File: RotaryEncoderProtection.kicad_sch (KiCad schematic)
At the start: 14 parts, among them J1 DE9_Plug_MountingHoles, J2 Conn_01x01, J3 Conn_01x04

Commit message: removed traces, where zones are; added text, logos, copyright; added Reichelt article numbvers
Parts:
- C1: Reichelt.de (none) -> X7R-G0805 100N
- C2: Reichelt.de (none) -> RAD 22/35
- D1: Reichelt.de (none) -> 1N 4148W DIO
- D2, D3, D4: Reichelt.de (none) -> SMD ZF 24
- J1: Reichelt.de (none) -> D-SUB ST 09US
- R1: Reichelt.de (none) -> SMD-0805 22,0
- R2, R3, R4, R5: Reichelt.de (none) -> SMD-0805 10,0K
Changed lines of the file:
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@@
+			)
+		)
+		(property "Reichelt.de" "SMD-0805 10,0K"
+			(at 83.82 63.5 0)
+			(effects
+				(font
+					(size 1.27 1.27)
+				)
+				(hide yes)
 			)
 		)
@@
 			)
 		)
+		(property "Reichelt.de" "SMD-0805 10,0K"
+			(at 118.11 53.34 0)
+			(effects
+				(font
+					(size 1.27 1.27)
+				)
+				(hide yes)
+			)
+		)
 		(pin "2"
 		)
@@
 			)
 		)
+		(property "Reichelt.de" "SMD ZF 24"
+			(at 118.11 77.47 90)
+			(effects
+				(font
+					(size 1.27 1.27)
+				)
+				(hide yes)
+			)
+		)
 		(pin "2"
 		)
@@
 			)
 		)
-		(property "Datasheet" "~"
+		(property "Datasheet" "https://cdn-reichelt.de/documents/datenblatt/C120/DBR1-MXX-L.pdf"
 			(at 62.23 68.58 0)
 			(effects
@@
 			)
 		)
+		(property "Reichelt.de" "D-SUB ST 09US"
+			(at 62.23 68.58 0)
+			(effects
+				(font
+					(size 1.27 1.27)
+				)
+				(hide yes)
+			)
+		)
 		(pin "0"
 		)
@@
 			)
 		)
+		(property "Reichelt.de" "X7R-G0805 100N"
+			(at 132.08 53.34 0)
+			(effects
+				(font
+					(size 1.27 1.27)
+				)
+				(hide yes)
+			)
+		)
 		(pin "1"
 		)
@@
 		)
 		(property "Description" "Resistor"
+			(at 83.82 71.12 0)
+			(effects
+				(font
+					(size 1.27 1.27)
+				)
+				(hide yes)
+			)
+		)
+		(property "Reichelt.de" "SMD-0805 10,0K"
 			(at 83.82 71.12 0)
 			(effects
@@
 			)
 		)
+		(property "Reichelt.de" "SMD-0805 22,0"
+			(at 96.52 43.18 0)
+			(effects
+				(font
+					(size 1.27 1.27)
+				)
+				(hide yes)
+			)
+		)
 		(pin "2"
 		)
@@
 			)
 		)
+		(property "Reichelt.de" "SMD ZF 24"
+			(at 156.21 53.34 90)
+			(effects
+				(font
+					(size 1.27 1.27)
+				)
+				(hide yes)
+			)
+		)
 		(pin "2"
 		)
@@
 			)
 		)
+		(property "Reichelt.de" "1N 4148W DIO"
+			(at 81.28 43.18 0)
+			(effects
+				(font
+					(size 1.27 1.27)
+				)
+				(hide yes)
+			)
+		)
 		(pin "1"
 		)
@@
 			)
 		)
+		(property "Reichelt.de" "RAD 22/35"
+			(at 144.78 53.34 0)
+			(effects
+				(font
+					(size 1.27 1.27)
+				)
+				(hide yes)
+			)
+		)
 		(pin "2"
 		)
@@
 			)
 		)
+		(property "Reichelt.de" "SMD-0805 10,0K"
+			(at 104.14 53.34 0)
+			(effects
+				(font
+					(size 1.27 1.27)
+				)
+				(hide yes)
+			)
+		)
 		(pin "2"
 		)
@@
 			(effects
 				(font
+					(size 1.27 1.27)
+				)
+				(hide yes)
+			)
+		)
+		(property "Reichelt.de" "SMD ZF 24"
+			(at 104.14 77.47 90)
+			(effects
+				(font

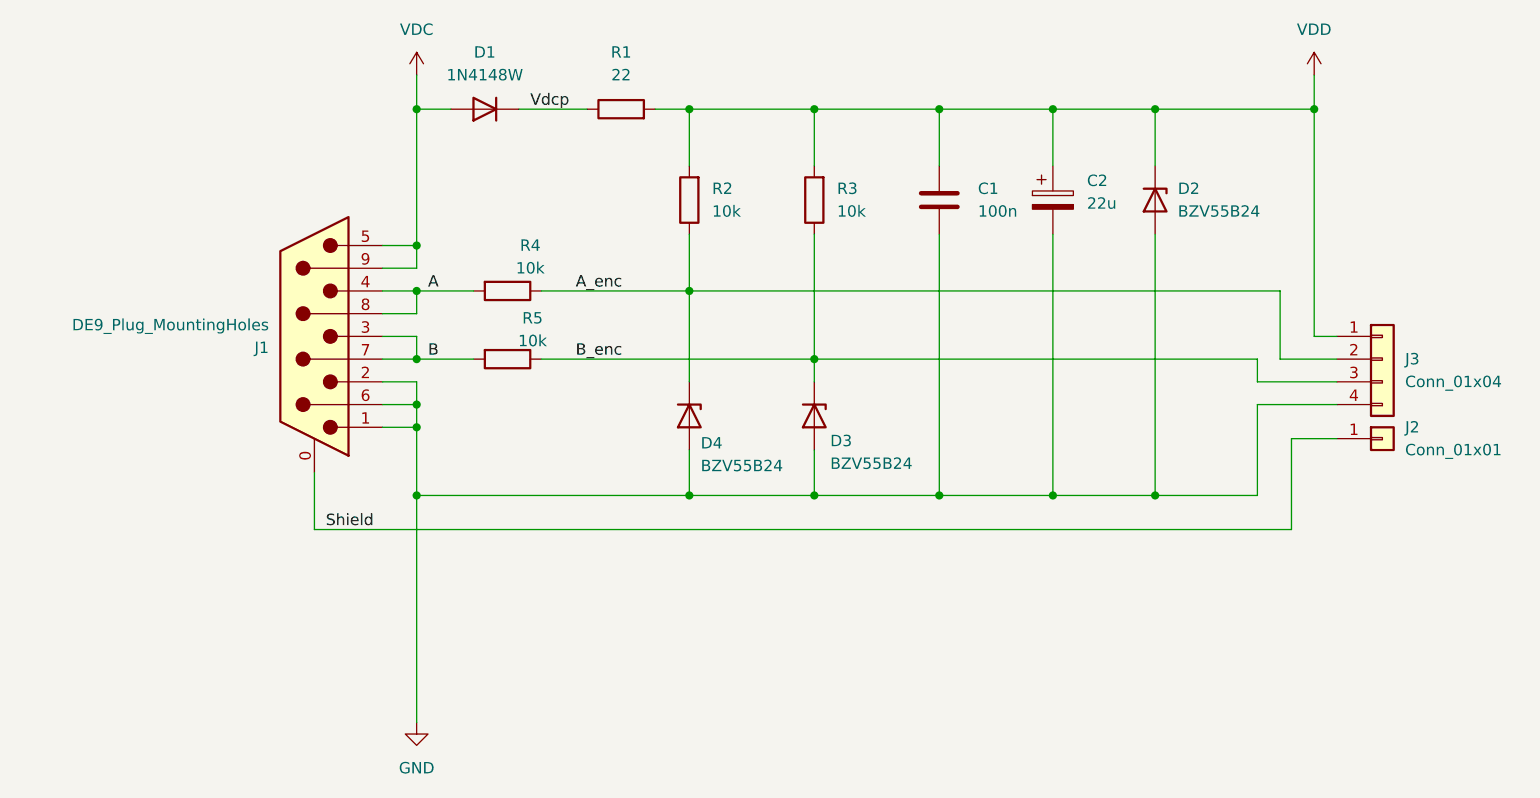
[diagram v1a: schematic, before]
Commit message: smaller board
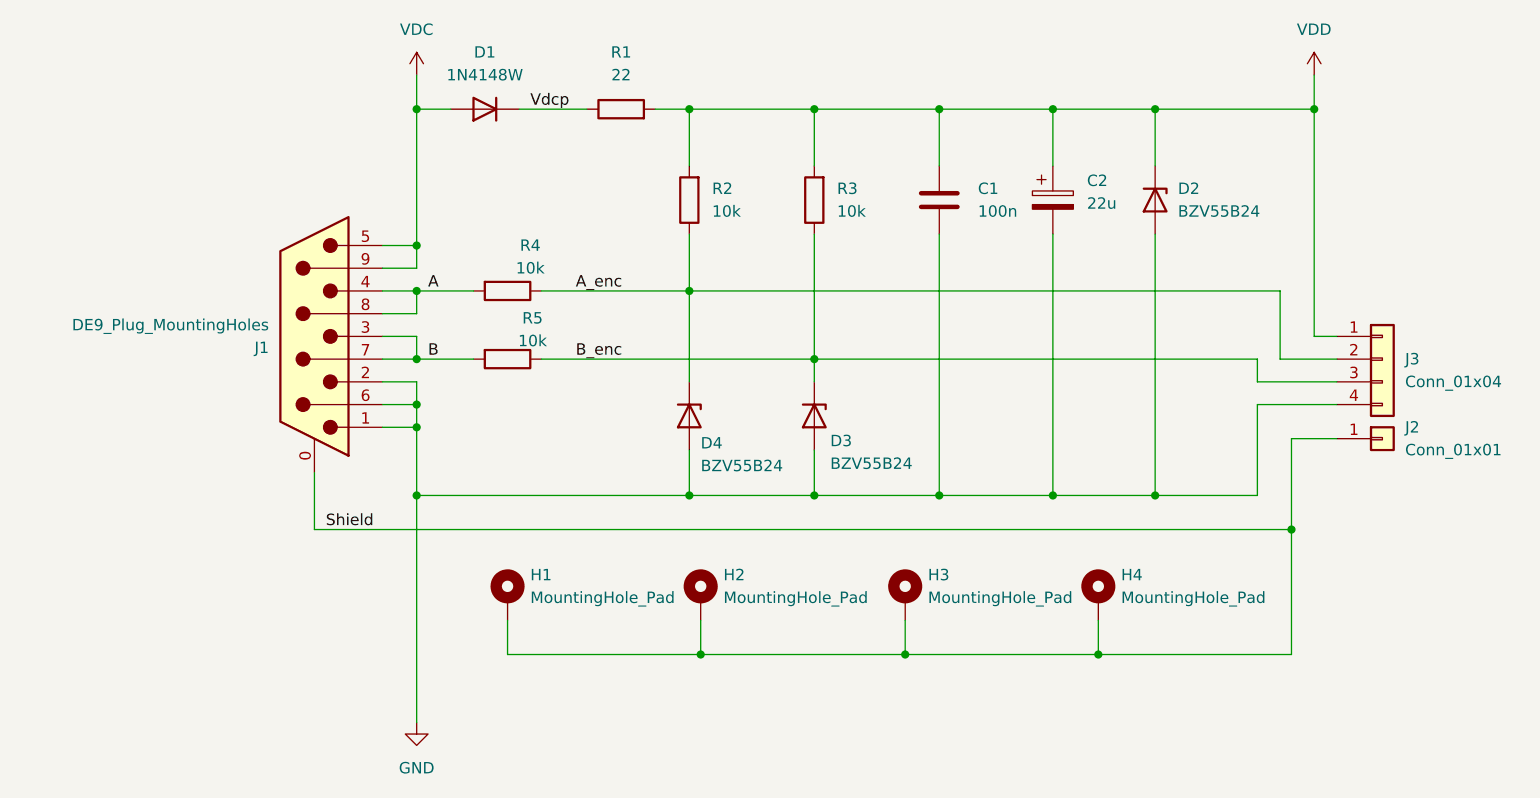
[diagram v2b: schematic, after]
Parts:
- added H1, H2, H3, H4: MountingHole_Pad, MountingHole:MountingHole_2.7mm_M2.5_ISO14580_Pad_TopBottom, symbol Mechanical:MountingHole_Pad
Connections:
- net Shield: now also H1.1, H2.1, H3.1, H4.1

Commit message: Digikey M3 D-Sub-9 Connector
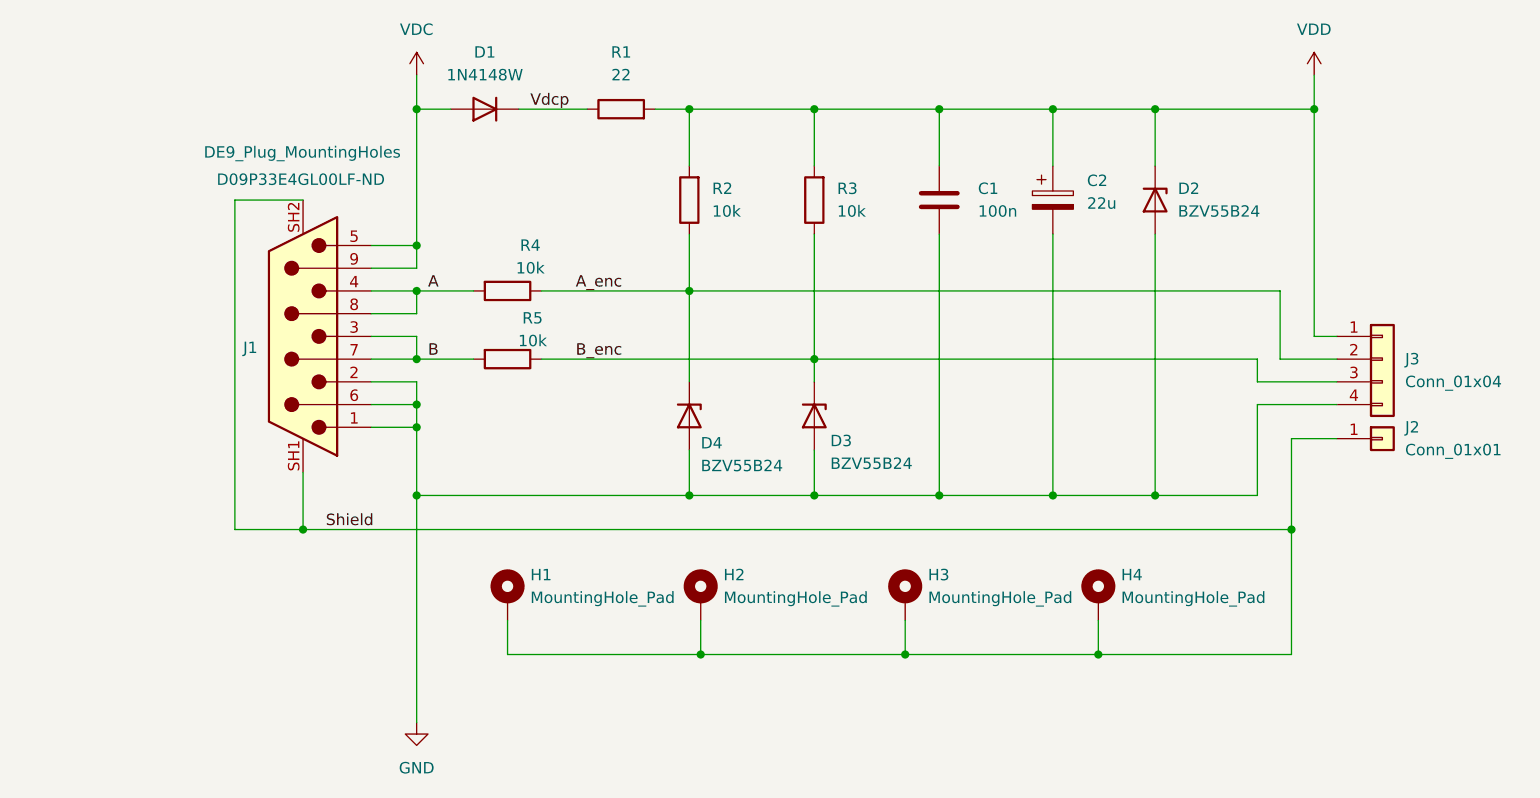
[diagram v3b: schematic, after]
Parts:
- J1: footprint Connector_Dsub:DSUB-9_Male_Horizontal_P2.77x2.84mm_EdgePinOffset4.94mm_Housed_MountingHolesOffset7.48mm -> D09P33E4GL00LF_b:AMPHENOL_D09P33E4GL00LF; Digikey.de (none) -> D09P33E4GL00LF-ND; Reichelt.de D-SUB ST 09US -> (none)
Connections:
- net Shield: now also J1.SH1 (PAD), J1.SH2 (PAD); no longer J1.0 (PAD)
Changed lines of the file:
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@@
 (kicad_sch
-	(version 20231120)
+	(version 20250114)
 	(generator "eeschema")
-	(generator_version "8.0")
+	(generator_version "9.0")
 	(paper "A4")
 	(title_block
@@
 	)
 	(junction
+		(at 60.96 90.17)
+		(diameter 0)
+		(color 0 0 0 0)
+	)
+	(junction
 		(at 73.66 76.2)
 		(diameter 0)
@@
 	(wire
 		(pts
+			(xy 53.34 53.34) (xy 53.34 90.17)
+		)
+		(stroke
+			(width 0)
+			(type default)
+		)
+	)
+	(wire
+		(pts
 			(xy 73.66 73.66) (xy 73.66 76.2)
 		)
@@
 	(wire
 		(pts
-			(xy 69.85 76.2) (xy 73.66 76.2)
+			(xy 68.58 76.2) (xy 73.66 76.2)
 		)
 		(stroke
@@
 	(wire
 		(pts
+			(xy 60.96 90.17) (xy 171.45 90.17)
+		)
+		(stroke
+			(width 0)
+			(type default)
+		)
+	)
+	(wire
+		(pts
 			(xy 104.14 43.18) (xy 104.14 49.53)
 		)
@@
 	(wire
 		(pts
-			(xy 69.85 66.04) (xy 73.66 66.04)
+			(xy 68.58 66.04) (xy 73.66 66.04)
 		)
 		(stroke
@@
 	(wire
 		(pts
-			(xy 69.85 58.42) (xy 73.66 58.42)
+			(xy 68.58 58.42) (xy 73.66 58.42)
 		)
 		(stroke
@@
 	(wire
 		(pts
-			(xy 69.85 68.58) (xy 73.66 68.58)
+			(xy 68.58 68.58) (xy 73.66 68.58)
+		)
+		(stroke
+			(width 0)
+			(type default)
+		)
+	)
+	(wire
+		(pts
+			(xy 53.34 90.17) (xy 60.96 90.17)
 		)
 		(stroke
@@
 	(wire
 		(pts
-			(xy 73.66 63.5) (xy 73.66 66.04)
+			(xy 73.66 66.04) (xy 73.66 63.5)
 		)
 		(stroke
@@
 	(wire
 		(pts
+			(xy 60.96 53.34) (xy 53.34 53.34)
+		)
+		(stroke
+			(width 0)
+			(type default)
+		)
+	)
+	(wire
+		(pts
 			(xy 83.82 104.14) (xy 83.82 100.33)
 		)
@@
 	(wire
 		(pts
-			(xy 69.85 78.74) (xy 73.66 78.74)
+			(xy 68.58 78.74) (xy 73.66 78.74)
 		)
 		(stroke
@@
 	(wire
 		(pts
-			(xy 69.85 71.12) (xy 73.66 71.12)
+			(xy 68.58 71.12) (xy 73.66 71.12)
 		)
 		(stroke
@@
 	(wire
 		(pts
-			(xy 62.23 90.17) (xy 171.45 90.17)
-		)
-		(stroke
-			(width 0)
-			(type default)
-		)
-	)
-	(wire
-		(pts
 			(xy 156.21 43.18) (xy 156.21 49.53)
 		)
@@
 	(wire
 		(pts
-			(xy 69.85 63.5) (xy 73.66 63.5)
+			(xy 68.58 63.5) (xy 73.66 63.5)
 		)
 		(stroke
@@
 	(wire
 		(pts
-			(xy 69.85 73.66) (xy 73.66 73.66)
+			(xy 68.58 73.66) (xy 73.66 73.66)
 		)
 		(stroke
@@
 	(wire
 		(pts
-			(xy 73.66 58.42) (xy 73.66 60.96)
-		)
-		(stroke
-			(width 0)
-			(type default)
-		)
-	)
-	(wire
-		(pts
-			(xy 73.66 60.96) (xy 69.85 60.96)
+			(xy 73.66 60.96) (xy 73.66 58.42)
+		)
+		(stroke
+			(width 0)
+			(type default)
+		)
+	)
+	(wire
+		(pts
+			(xy 73.66 60.96) (xy 68.58 60.96)
 		)
 		(stroke
@@
 	(wire
 		(pts
-			(xy 62.23 83.82) (xy 62.23 90.17)
+			(xy 60.96 83.82) (xy 60.96 90.17)
 		)
 		(stroke
@@
 	(label "Shield"
 		(at 63.5 90.17 0)
-		(fields_autoplaced yes)
 		(effects
 			(font
@@
 	(label "Vdcp"
 		(at 86.36 43.18 0)
-		(fields_autoplaced yes)
 		(effects
 			(font
@@
 	(label "A"
 		(at 74.93 63.5 0)
-		(fields_autoplaced yes)
 		(effects
 			(font
@@
 	(label "A_enc"
 		(at 91.44 63.5 0)
-		(fields_autoplaced yes)
 		(effects
 			(font
@@
 	(label "B"
 		(at 74.93 71.12 0)
-		(fields_autoplaced yes)
 		(effects
 			(font
@@
 	(label "B_enc"
 		(at 91.44 71.12 0)
-		(fields_autoplaced yes)
 		(effects
 			(font
@@
 	(symbol
 		(lib_id "Connector:DE9_Plug_MountingHoles")
-		(at 62.23 68.58 0)
+		(at 60.96 68.58 0)
 		(mirror y)
 		(unit 1)
@@
 		(dnp no)
 		(property "Reference" "J1"
-			(at 57.15 69.8501 0)
+			(at 55.88 69.8501 0)
 			(effects
 				(font
@@
 		)
 		(property "Value" "DE9_Plug_MountingHoles"
-			(at 57.15 67.3101 0)
+			(at 71.882 48.006 0)
 			(effects
 				(font
@@
 			)
 		)
-		(property "Footprint" "Connector_Dsub:DSUB-9_Male_Horizontal_P2.77x2.84mm_EdgePinOffset4.94mm_Housed_MountingHolesOffset7.48mm"
-			(at 62.23 68.58 0)
+		(property "Footprint" "D09P33E4GL00LF_b:AMPHENOL_D09P33E4GL00LF"
+			(at 60.96 68.58 0)
 			(effects
 				(font
@@
 		)
 		(property "Datasheet" "https://cdn-reichelt.de/documents/datenblatt/C120/DBR1-MXX-L.pdf"
-			(at 62.23 68.58 0)
+			(at 60.96 68.58 0)
 			(effects
 				(font
@@
 		)
 		(property "Description" "9-pin male plug pin D-SUB connector, Mounting Hole"
-			(at 62.23 68.58 0)
-			(effects
-				(font
-					(size 1.27 1.27)
-				)
-				(hide yes)
-			)
-		)
-		(property "Reichelt.de" "D-SUB ST 09US"
-			(at 62.23 68.58 0)
-			(effects
-				(font
-					(size 1.27 1.27)
-				)
-				(hide yes)
-			)
-		)
-		(pin "0"
+			(at 60.96 68.58 0)
+			(effects
+				(font
+					(size 1.27 1.27)
+				)
+				(hide yes)
+			)
+		)
+		(property "Digikey.de" "D09P33E4GL00LF-ND"
+			(at 60.706 51.054 0)
+			(effects
+				(font
+					(size 1.27 1.27)
+				)
+			)
+		)
+		(pin "SH1"
 		)
 		(pin "8"
@@
 		)
 		(pin "6"
+		)
+		(pin "SH2"
 		)
 		(instances
@@
 		)
 	)
+	(embedded_fonts no)
 )

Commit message: new KiCad Standard D-Sub-9 Connector
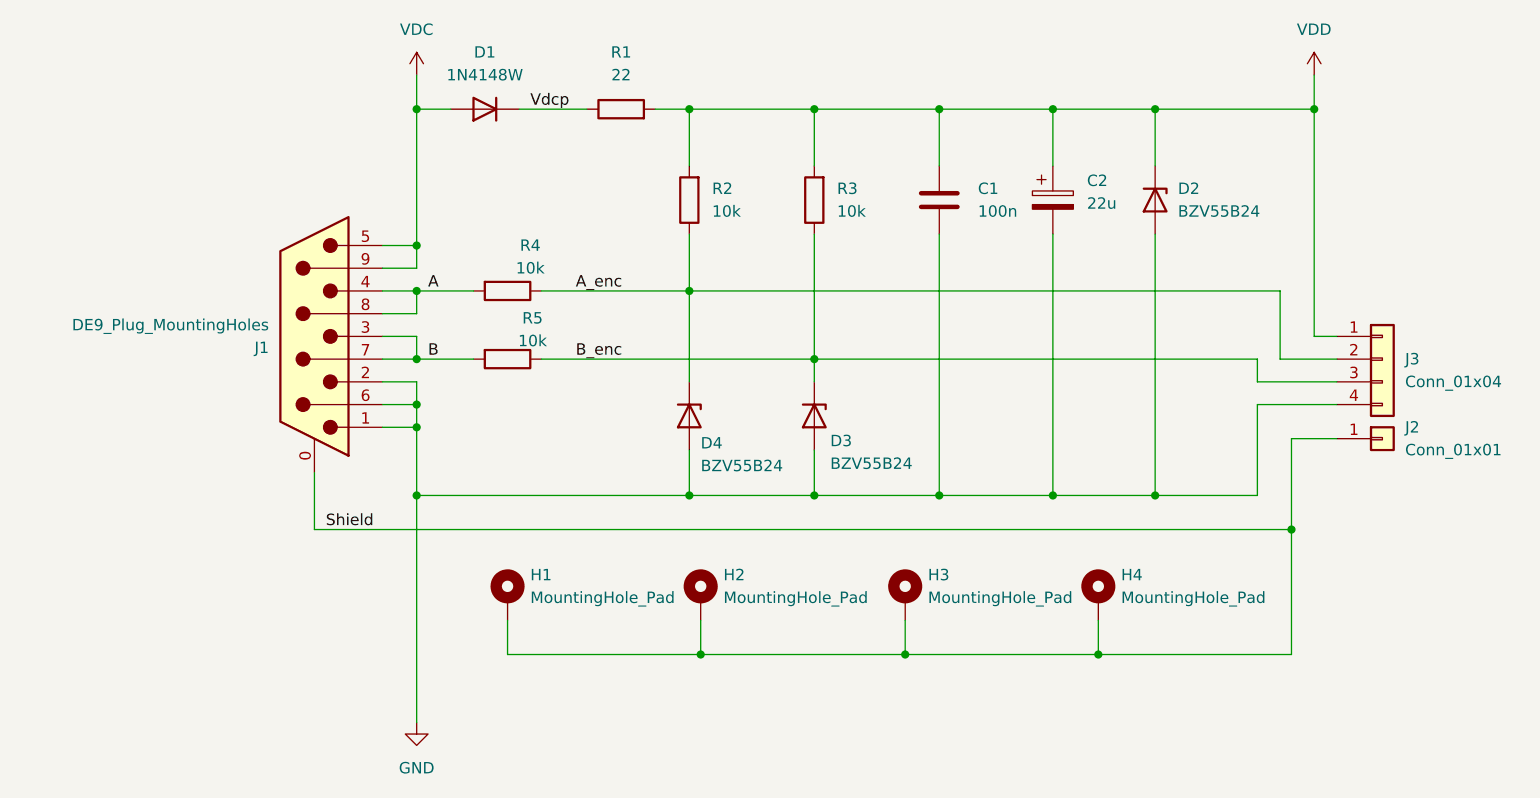
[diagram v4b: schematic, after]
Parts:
- J1: footprint D09P33E4GL00LF_b:AMPHENOL_D09P33E4GL00LF -> Connector_Dsub:DSUB-9_Pins_Horizontal_P2.77x2.84mm_EdgePinOffset7.70mm_Housed_MountingHolesOffset9.12mm; Digikey.de D09P33E4GL00LF-ND -> (none); Reichelt.de (none) -> D-SUB ST 09US
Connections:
- net Shield: now also J1.0 (PAD); no longer J1.SH1 (PAD), J1.SH2 (PAD)
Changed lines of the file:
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@@
-	)
-	(junction
-		(at 60.96 90.17)
-		(diameter 0)
-		(color 0 0 0 0)
 	)
 	(junction
@@
 	(wire
 		(pts
-			(xy 53.34 53.34) (xy 53.34 90.17)
-		)
-		(stroke
-			(width 0)
-			(type default)
-		)
-	)
-	(wire
-		(pts
 			(xy 73.66 73.66) (xy 73.66 76.2)
 		)
@@
 	(wire
 		(pts
-			(xy 68.58 76.2) (xy 73.66 76.2)
+			(xy 69.85 76.2) (xy 73.66 76.2)
 		)
 		(stroke
@@
 	(wire
 		(pts
-			(xy 60.96 90.17) (xy 171.45 90.17)
-		)
-		(stroke
-			(width 0)
-			(type default)
-		)
-	)
-	(wire
-		(pts
 			(xy 104.14 43.18) (xy 104.14 49.53)
 		)
@@
 	(wire
 		(pts
-			(xy 68.58 66.04) (xy 73.66 66.04)
+			(xy 69.85 66.04) (xy 73.66 66.04)
 		)
 		(stroke
@@
 	(wire
 		(pts
-			(xy 68.58 58.42) (xy 73.66 58.42)
+			(xy 69.85 58.42) (xy 73.66 58.42)
 		)
 		(stroke
@@
 	(wire
 		(pts
-			(xy 68.58 68.58) (xy 73.66 68.58)
-		)
-		(stroke
-			(width 0)
-			(type default)
-		)
-	)
-	(wire
-		(pts
-			(xy 53.34 90.17) (xy 60.96 90.17)
+			(xy 69.85 68.58) (xy 73.66 68.58)
 		)
 		(stroke
@@
 	(wire
 		(pts
-			(xy 73.66 66.04) (xy 73.66 63.5)
+			(xy 73.66 63.5) (xy 73.66 66.04)
 		)
 		(stroke
@@
 	(wire
 		(pts
-			(xy 60.96 53.34) (xy 53.34 53.34)
-		)
-		(stroke
-			(width 0)
-			(type default)
-		)
-	)
-	(wire
-		(pts
 			(xy 83.82 104.14) (xy 83.82 100.33)
 		)
@@
 	(wire
 		(pts
-			(xy 68.58 78.74) (xy 73.66 78.74)
+			(xy 69.85 78.74) (xy 73.66 78.74)
 		)
 		(stroke
@@
 	(wire
 		(pts
-			(xy 68.58 71.12) (xy 73.66 71.12)
+			(xy 69.85 71.12) (xy 73.66 71.12)
 		)
 		(stroke
@@
 	(wire
 		(pts
+			(xy 62.23 90.17) (xy 171.45 90.17)
+		)
+		(stroke
+			(width 0)
+			(type default)
+		)
+	)
+	(wire
+		(pts
 			(xy 156.21 43.18) (xy 156.21 49.53)
 		)
@@
 	(wire
 		(pts
-			(xy 68.58 63.5) (xy 73.66 63.5)
+			(xy 69.85 63.5) (xy 73.66 63.5)
 		)
 		(stroke
@@
 	(wire
 		(pts
-			(xy 68.58 73.66) (xy 73.66 73.66)
+			(xy 69.85 73.66) (xy 73.66 73.66)
 		)
 		(stroke
@@
 	(wire
 		(pts
-			(xy 73.66 60.96) (xy 73.66 58.42)
-		)
-		(stroke
-			(width 0)
-			(type default)
-		)
-	)
-	(wire
-		(pts
-			(xy 73.66 60.96) (xy 68.58 60.96)
+			(xy 73.66 58.42) (xy 73.66 60.96)
+		)
+		(stroke
+			(width 0)
+			(type default)
+		)
+	)
+	(wire
+		(pts
+			(xy 73.66 60.96) (xy 69.85 60.96)
 		)
 		(stroke
@@
 	(wire
 		(pts
-			(xy 60.96 83.82) (xy 60.96 90.17)
+			(xy 62.23 83.82) (xy 62.23 90.17)
 		)
 		(stroke
@@
 	(symbol
 		(lib_id "Connector:DE9_Plug_MountingHoles")
-		(at 60.96 68.58 0)
+		(at 62.23 68.58 0)
 		(mirror y)
 		(unit 1)
@@
 		(dnp no)
 		(property "Reference" "J1"
-			(at 55.88 69.8501 0)
+			(at 57.15 69.8501 0)
 			(effects
 				(font
@@
 		)
 		(property "Value" "DE9_Plug_MountingHoles"
-			(at 71.882 48.006 0)
+			(at 57.15 67.3101 0)
 			(effects
 				(font
@@
 			)
 		)
-		(property "Footprint" "D09P33E4GL00LF_b:AMPHENOL_D09P33E4GL00LF"
-			(at 60.96 68.58 0)
+		(property "Footprint" "Connector_Dsub:DSUB-9_Pins_Horizontal_P2.77x2.84mm_EdgePinOffset7.70mm_Housed_MountingHolesOffset9.12mm"
+			(at 62.23 68.58 0)
 			(effects
 				(font
@@
 		)
 		(property "Datasheet" "https://cdn-reichelt.de/documents/datenblatt/C120/DBR1-MXX-L.pdf"
-			(at 60.96 68.58 0)
+			(at 62.23 68.58 0)
 			(effects
 				(font
@@
 		)
 		(property "Description" "9-pin male plug pin D-SUB connector, Mounting Hole"
-			(at 60.96 68.58 0)
-			(effects
-				(font
-					(size 1.27 1.27)
-				)
-				(hide yes)
-			)
-		)
-		(property "Digikey.de" "D09P33E4GL00LF-ND"
-			(at 60.706 51.054 0)
-			(effects
-				(font
-					(size 1.27 1.27)
-				)
-			)
-		)
-		(pin "SH1"
+			(at 62.23 68.58 0)
+			(effects
+				(font
+					(size 1.27 1.27)
+				)
+				(hide yes)
+			)
+		)
+		(property "Reichelt.de" "D-SUB ST 09US"
+			(at 62.23 68.58 0)
+			(effects
+				(font
+					(size 1.27 1.27)
+				)
+				(hide yes)
+			)
+		)
+		(pin "0"
 		)
 		(pin "8"
@@
 		(pin "6"
 		)
-		(pin "SH2"
-		)
 		(instances

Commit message: replaced Reichelt SKU for D-Sub-9 Connector
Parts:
- J1: Reichelt.de D-SUB ST 09US -> D-SUB ST 09EU
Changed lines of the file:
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@@
 			)
 		)
-		(property "Reichelt.de" "D-SUB ST 09US"
+		(property "Reichelt.de" "D-SUB ST 09EU"
 			(at 62.23 68.58 0)
 			(effects
